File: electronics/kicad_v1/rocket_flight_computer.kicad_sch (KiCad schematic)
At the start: 4 parts, among them IC1 ADXL375, U1 Teensy4.1, U2 BMP390L, U3 BMI088

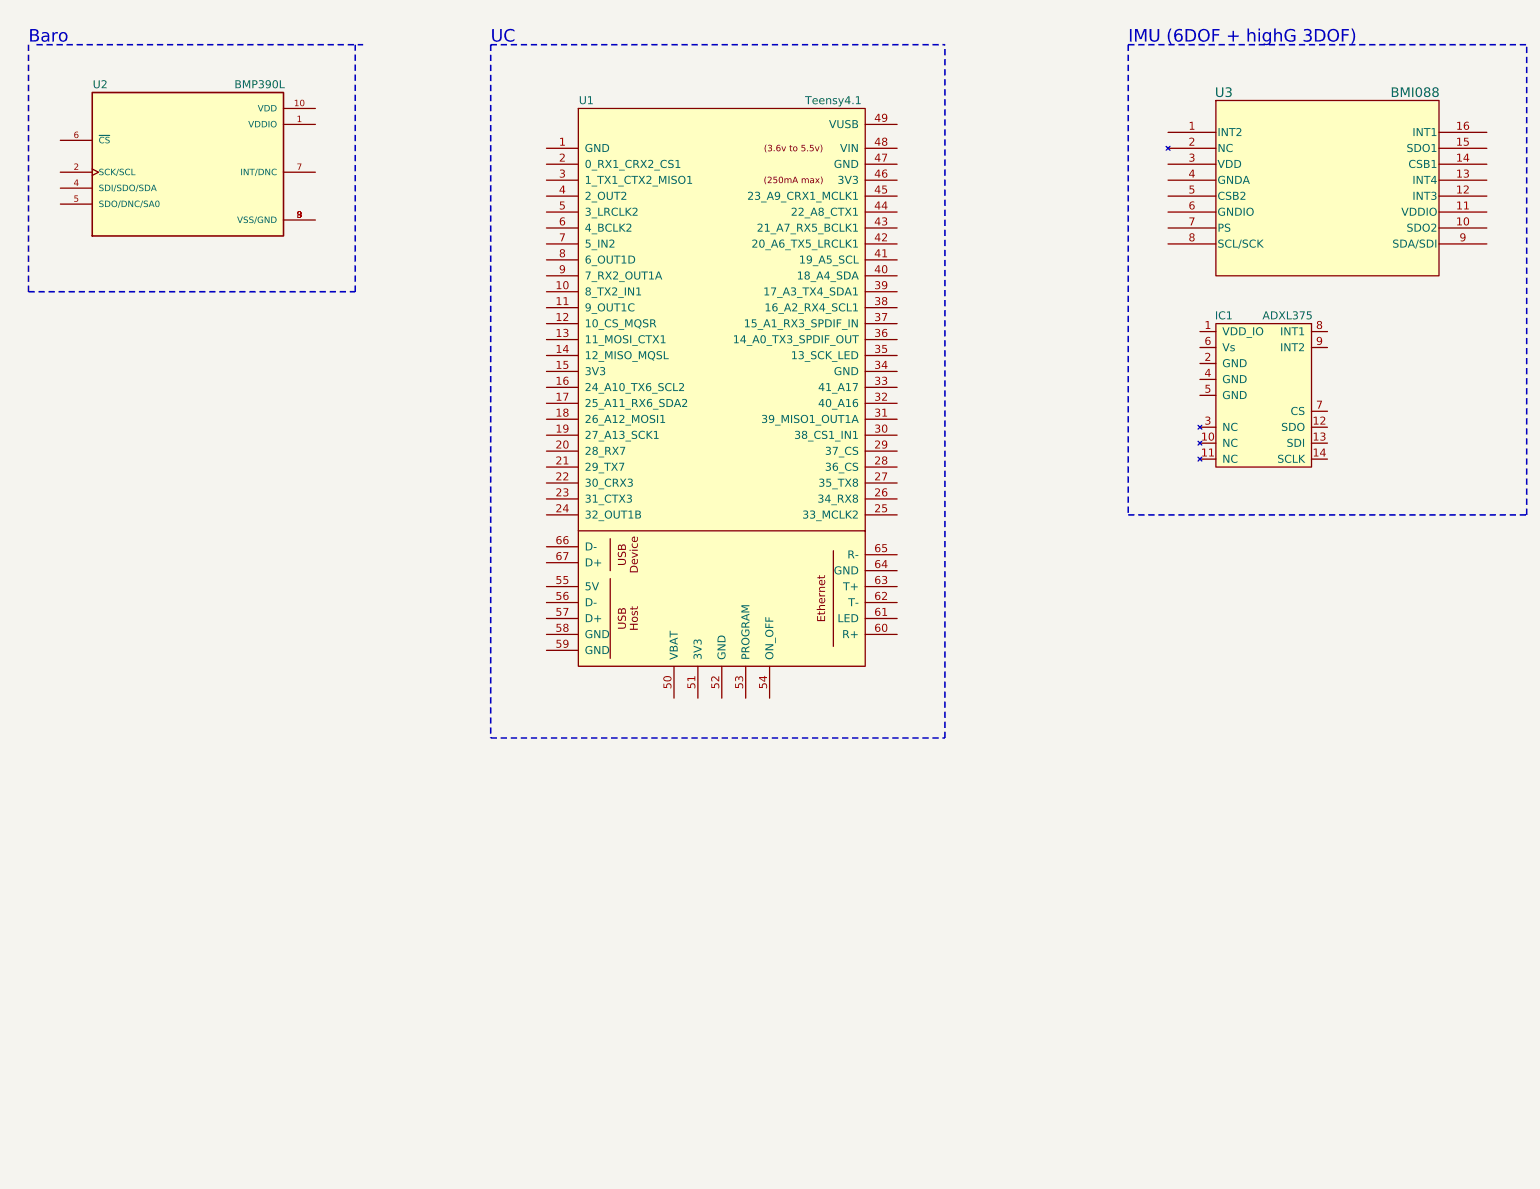
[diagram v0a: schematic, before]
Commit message: schematic for barometer
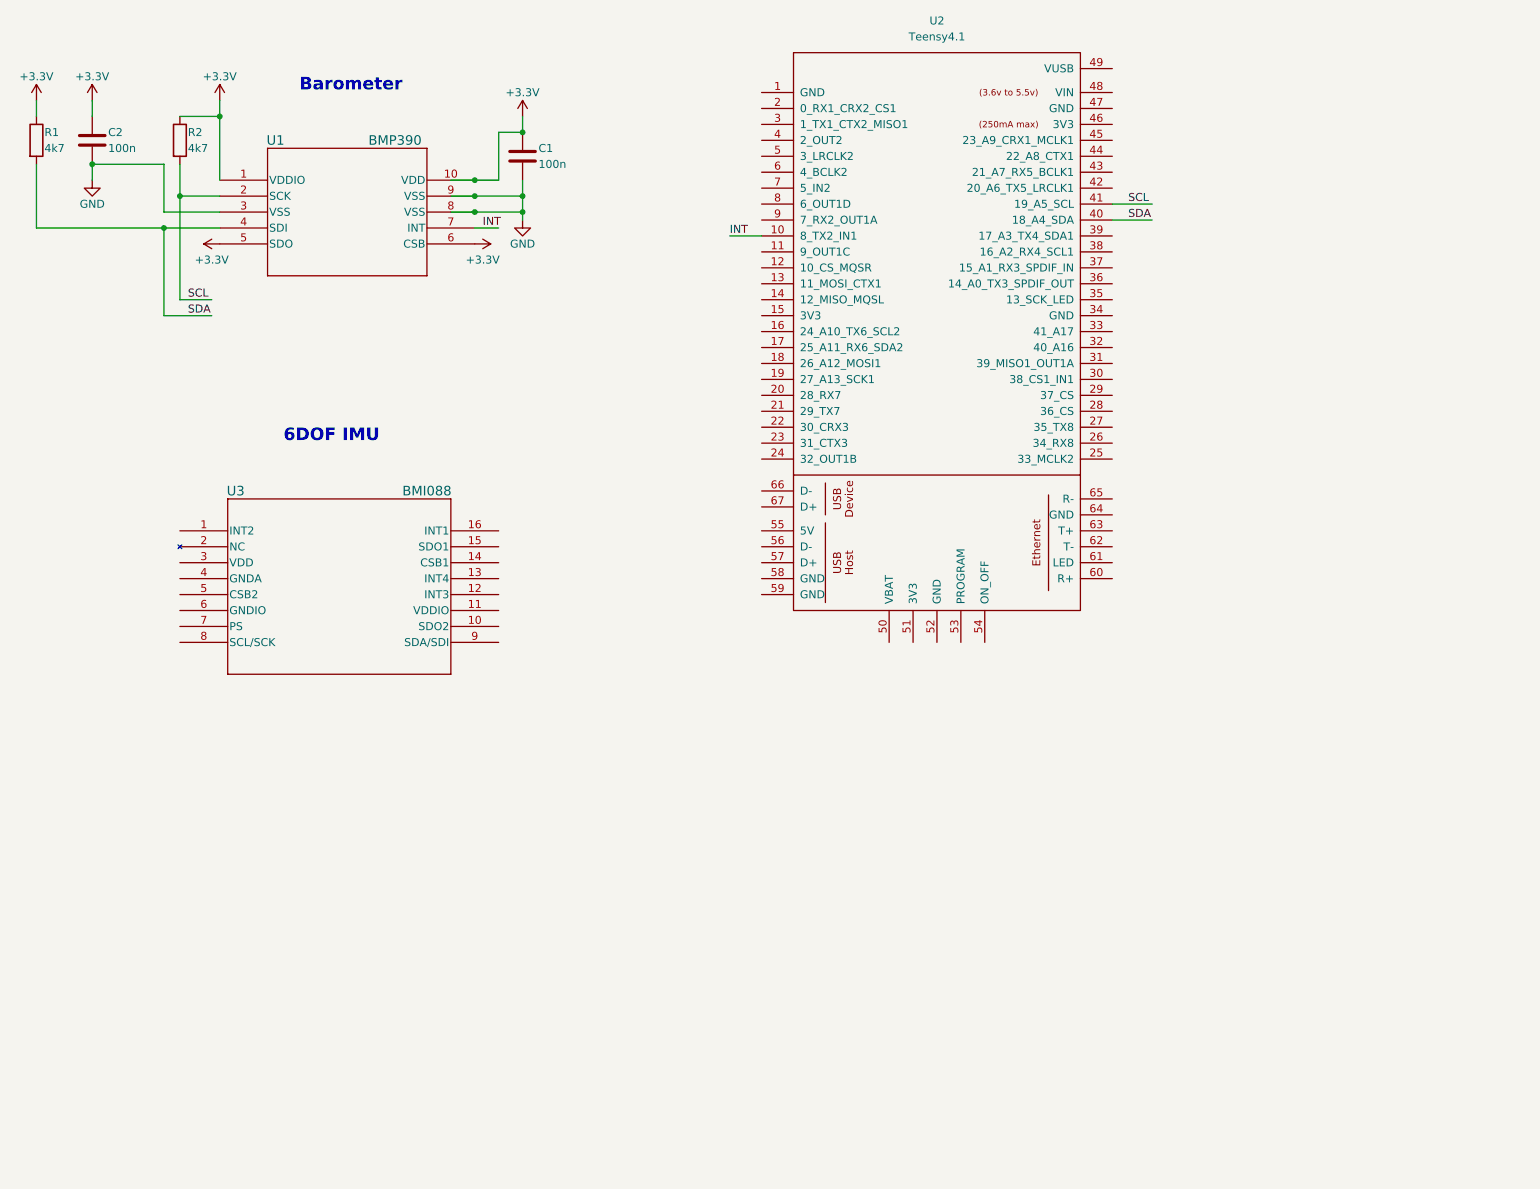
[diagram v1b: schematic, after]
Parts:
- removed IC1: ADXL375, agg:ADXL3x5, symbol adxl375:ADXL375
- removed U1: Teensy4.1, symbol teensy:Teensy4.1
- removed U2: BMP390L, BMP390L:XDCR_BMP390L, symbol BMP390L:BMP390L
- added C1, C2: 100n, symbol Device:C
- added R1, R2: 4k7, symbol Device:R
- added U1: BMP390, LGA10_BMP390_BOS, symbol bmp390:BMP390
- added U2: Teensy4.1, symbol teensy:Teensy4.1
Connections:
- new net +3.3V: C1.1, C2.1, R1.1, R2.1, U1.1 (VDDIO), U1.10 (VDD), U1.5 (SDO), U1.6 (CSB)
- new net GND: C1.2, C2.2, U1.3 (VSS), U1.8 (VSS), U1.9 (VSS)
- new net INT: U1.7 (INT), U2.10 (8_TX2_IN1)
- new net SCL: R2.2, U1.2 (SCK), U2.41 (19_A5_SCL)
- new net SDA: R1.2, U1.4 (SDI), U2.40 (18_A4_SDA)
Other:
- note added: "6DOF IMU"
- note added: "Barometer"
- note removed: "Baro"
- note removed: "IMU (6DOF + highG 3DOF)"
- note removed: "UC"

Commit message: add IMU schematic
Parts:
- added C3, C4: 100n, symbol Device:C
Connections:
- net +3.3V: now also U2.6 (4_BCLK2), U3.11 (VDDIO), U3.14 (CSB1), U3.3 (VDD), U3.7 (PS), C3.1, C4.1
- net GND: now also U3.4 (GNDA), U3.6 (GNDIO), C3.2, C4.2
- net INT2_ACCEL: now reaches U3.1 (INT2)
- net INT2_ACCEL: now also U2.7 (5_IN2)
- net A0_GYRO: now reaches U3.10 (SDO2)
- net A0_GYRO: now also U2.32 (40_A16)
- net INT3_GYRO: now reaches U3.12 (INT3)
- net INT3_GYRO: now also U2.5 (3_LRCLK2)
- net A0_ACCEL: now reaches U3.15 (SDO1)
- net A0_ACCEL: now also U2.33 (41_A17)
- net INT1_ACCEL: now reaches U3.16 (INT1)
- net INT1_ACCEL: now also U2.4 (2_OUT2)
- net SCL1: now reaches U3.8 (SCL/SCK)
- net SCL1: now also U2.38 (16_A2_RX4_SCL1)
- net SDA1: now reaches U3.9 (SDA/SDI)
- net SDA1: now also U2.39 (17_A3_TX4_SDA1)
- no-connect marks 0 -> 1
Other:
- note added: "Microcontroller"
- moved on the sheet: C2, R1, U2, U3

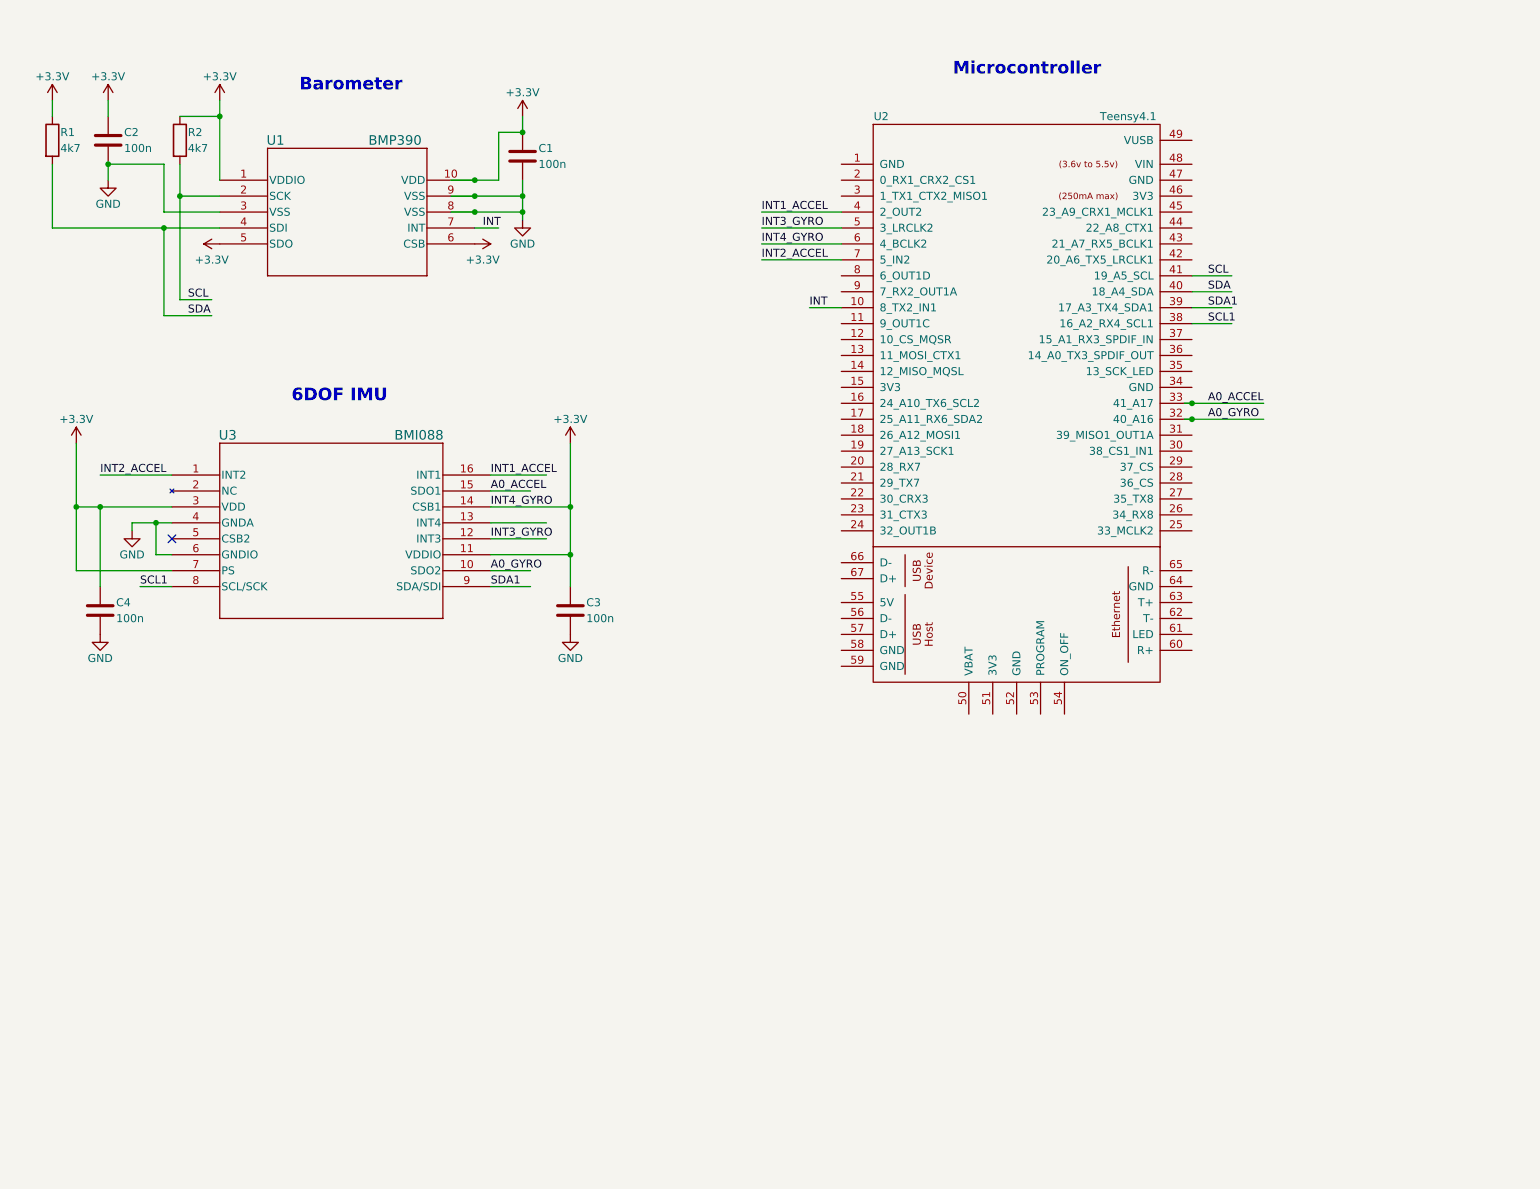
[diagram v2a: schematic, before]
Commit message: change symbol libs, hook up power to 3V3, add RF symbol
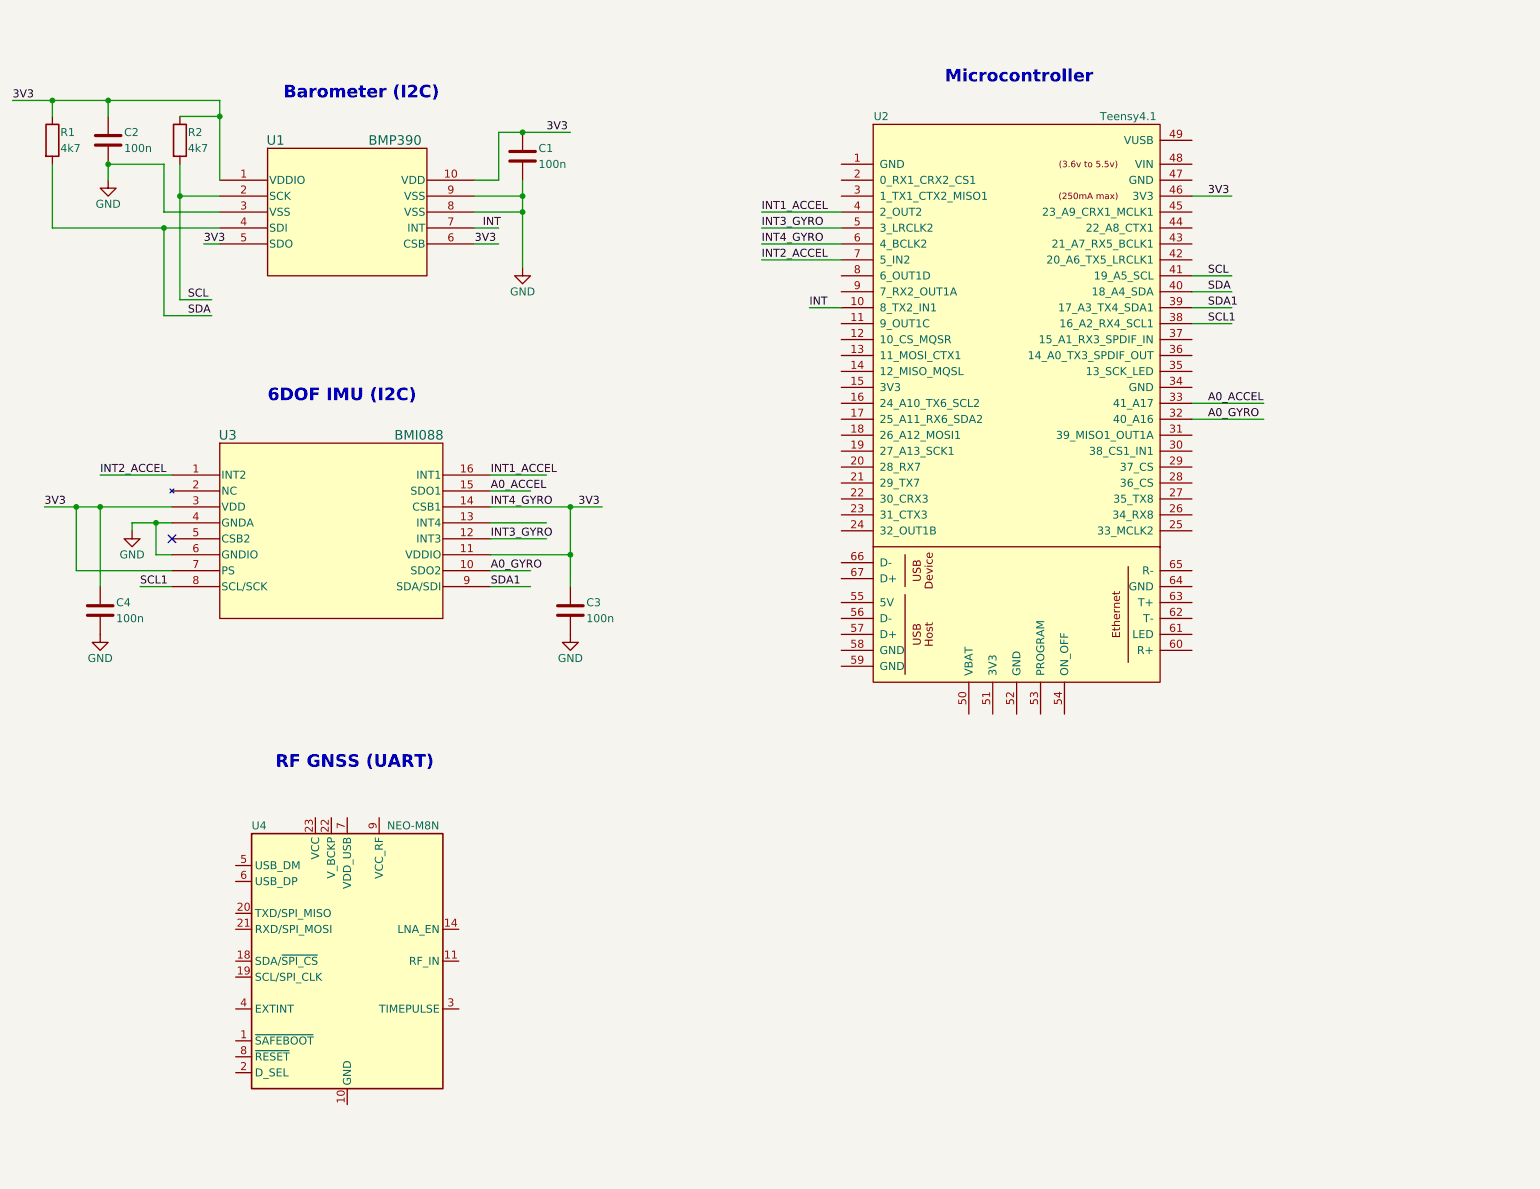
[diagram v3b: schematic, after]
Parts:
- added U4: NEO-M8N, RF_GPS:ublox_NEO, symbol RF_GPS:NEO-M8N
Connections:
- net +3.3V is gone; now on net 3V3: C1.1, C2.1, C3.1, C4.1, R1.1, R2.1, U1.1 (VDDIO), U1.10 (VDD), U1.5 (SDO), U1.6 (CSB), U2.6 (4_BCLK2), U3.11 (VDDIO), U3.14 (CSB1), U3.3 (VDD), U3.7 (PS)
- net 3V3: now reaches U2.46 (3V3)
- new net: U4.10 (GND), U4.12 (GND), U4.13 (GND), U4.24 (GND)
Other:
- note added: "6DOF IMU (I2C)"
- note added: "Barometer (I2C)"
- note added: "RF GNSS (UART)"
- note removed: "6DOF IMU"
- note removed: "Barometer"

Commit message: add RF component
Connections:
- net 3V3: now also U4.22 (V_BCKP), U4.23 (VCC)
- net GND: now also U2.1 (GND), U2.34 (GND), U2.47 (GND), U2.52 (GND), U4.10 (GND), U4.12 (GND), U4.13 (GND), U4.24 (GND), U4.7 (VDD_USB)
- net RX1: now reaches U2.2 (0_RX1_CRX2_CS1)
- net RX1: now also U4.21 (RXD/SPI_MOSI)
- net TX1: now reaches U2.3 (1_TX1_CTX2_MISO1)
- net TX1: now also U4.20 (TXD/SPI_MISO)
- no-connect marks 1 -> 19
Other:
- moved on the sheet: U4
